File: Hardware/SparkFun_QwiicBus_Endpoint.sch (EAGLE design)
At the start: 39 parts, among them J1 QWIIC, J2 QWIIC, J3 RJ45, U1 PCA9615

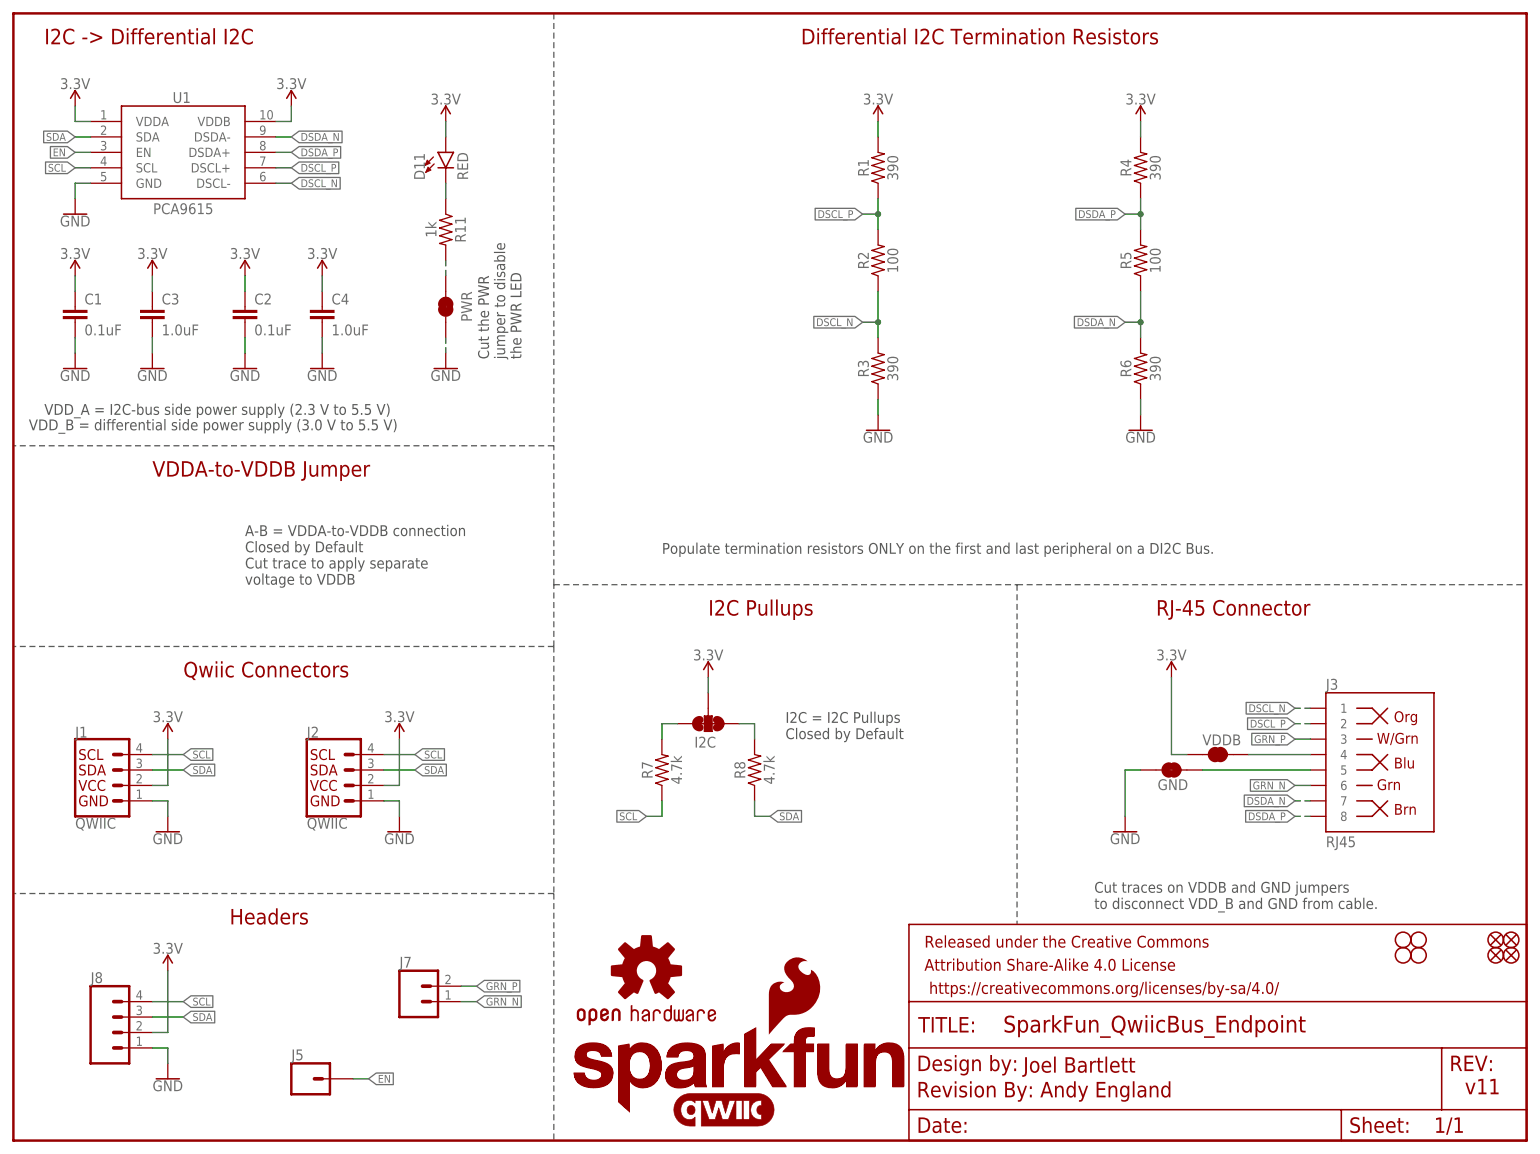
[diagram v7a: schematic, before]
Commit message: removing blue pair access
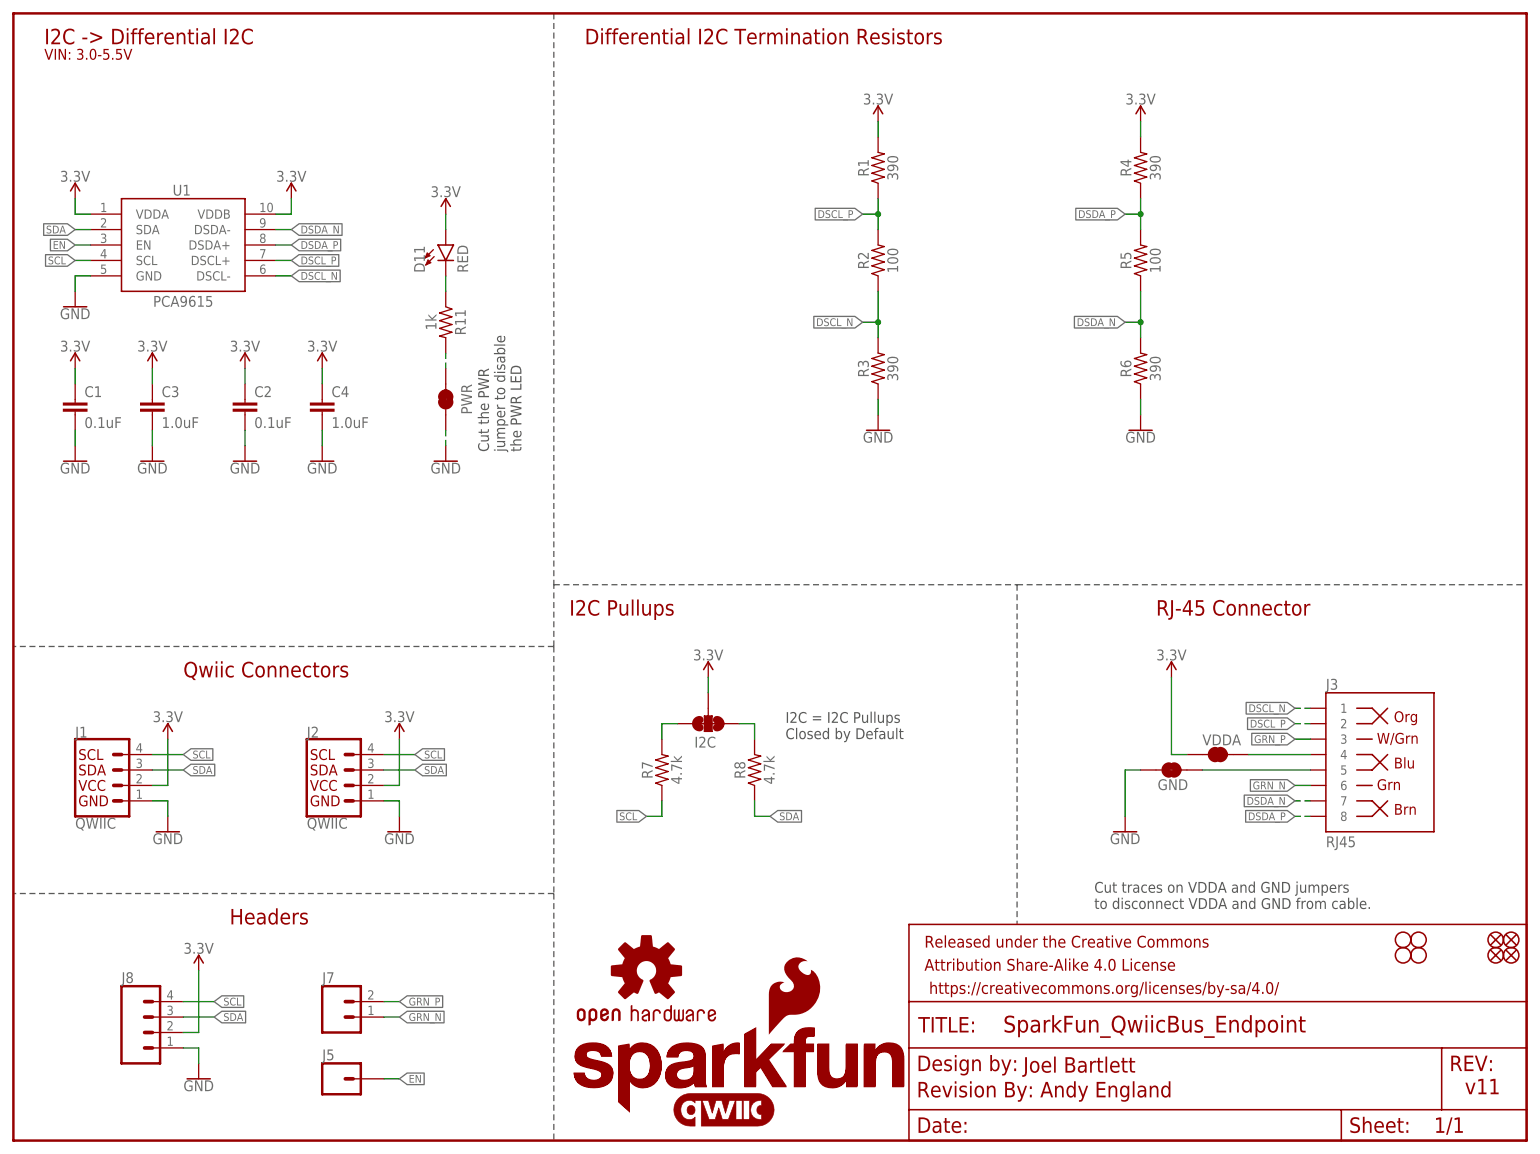
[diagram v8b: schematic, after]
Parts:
- renumbered VDDB to VDDA
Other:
- note added: "Cut traces on VDDA and GND jumpers to disconnect VDDA and GND from cable."
- note added: "VIN: 3.0-5.5V"
- note removed: "A-B = VDDA-to-VDDB connection Closed by Default Cut trace to apply separate voltage to VDDB"
- note removed: "Cut traces on VDDB and GND jumpers to disconnect VDD_B and GND from cable."
- note removed: "Populate termination resistors ONLY on the first and last peripheral on a DI2C Bus."
- note removed: "VDDA-to-VDDB Jumper"
- note removed: "VDD_A = I2C-bus side power supply (2.3 V to 5.5 V)"
- note removed: "VDD_B = differential side power supply (3.0 V to 5.5 V)"
- moved on the sheet: C1, C2, C3, C4, D11, J5, J7, J8, PWR, R11, U1
